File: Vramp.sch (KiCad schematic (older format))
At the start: 2 parts

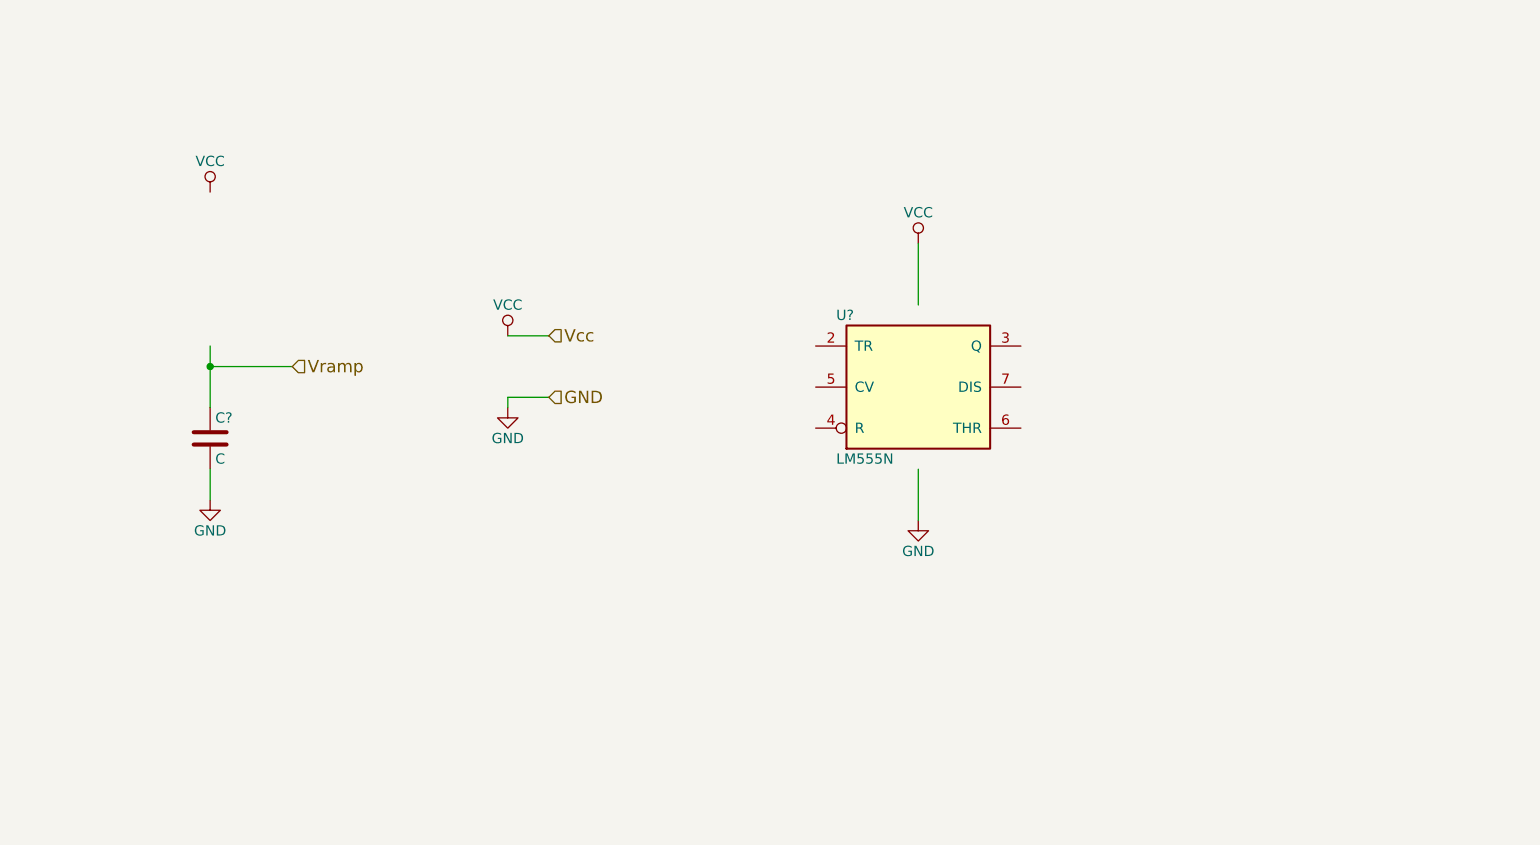
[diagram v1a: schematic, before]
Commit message: Created Ramp Voltage Source
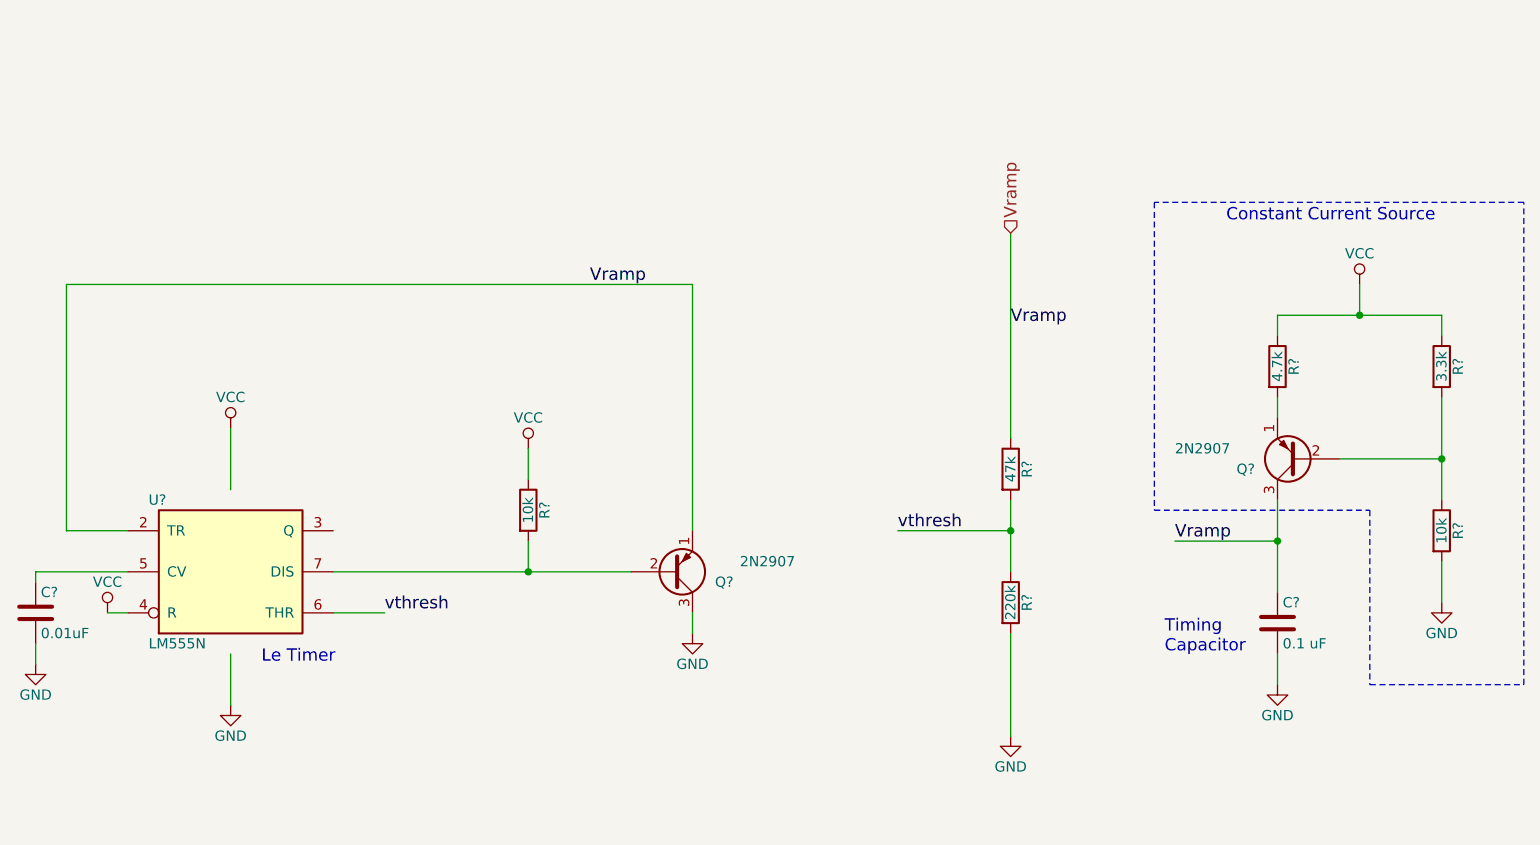
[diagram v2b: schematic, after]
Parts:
- added C?: 0.01uF, symbol C
- added Q? (x2): 2N2907, symbol Q_PNP_EBC
- added R? (x2): 10k, symbol R
- added R?: 4.7k, symbol R
- added R?: 3.3k, symbol R
- added R?: 47k, symbol R
- added R?: 220k, symbol R
- C?: value C -> 0.1 uF
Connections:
- net labels added: vthresh
- net labels removed: Vcc
- wire segments 8 -> 30
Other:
- note added: "Constant Current Source\n"
- note added: "Le Timer\n"
- note added: "Timing\nCapacitor\n"
- moved on the sheet: C?, U?

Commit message: Added some text to make things more obvious
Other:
- note added: "Charge Dumping\nCapacitor"
- moved on the sheet: C?, Q?, R?, U?

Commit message: Did a whole bunch of layout
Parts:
- C1, C2: renamed from C?; footprint (none) -> Capacitors_THT:C_Disc_D3_P2.5
- Q1, Q2: renamed from Q?; footprint (none) -> TO_SOT_Packages_THT:TO-18_3Pin
- R10, R11, R6, R7, R8, R9: renamed from R?; footprint (none) -> Resistors_THT:Resistor_Horizontal_RM7mm
- U4: renamed from U?; footprint (none) -> Housings_DIP:DIP-8_W7.62mm_LongPads
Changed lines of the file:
@@
 $Descr A4 11693 8268
 encoding utf-8
-Sheet 4 4
+Sheet 3 4
 Title ""
 Date ""
@@
 $EndDescr
 $Comp
-L GND #PWR?
+L GND #PWR012
 U 1 1 58B660FA
 P 8250 3850
-F 0 "#PWR?" H 8250 3600 50  0001 C CNN
+F 0 "#PWR012" H 8250 3600 50  0001 C CNN
 F 1 "GND" H 8250 3700 50  0000 C CNN
 F 2 "" H 8250 3850 50  0000 C CNN
@@
 $EndComp
 $Comp
-L C C?
+L C C2
 U 1 1 58B6610E
 P 8250 3550
-F 0 "C?" H 8275 3650 50  0000 L CNN
+F 0 "C2" H 8275 3650 50  0000 L CNN
 F 1 "0.1 uF" H 8275 3450 50  0000 L CNN
-F 2 "" H 8288 3400 50  0000 C CNN
+F 2 "Capacitors_THT:C_Disc_D3_P2.5" H 8288 3400 50  0001 C CNN
 F 3 "" H 8250 3550 50  0000 C CNN
 	1    8250 3550
@@
 	8250 2950 8250 3400
 $Comp
-L VCC #PWR?
+L VCC #PWR013
 U 1 1 58B662CB
 P 8650 1900
-F 0 "#PWR?" H 8650 1750 50  0001 C CNN
+F 0 "#PWR013" H 8650 1750 50  0001 C CNN
 F 1 "VCC" H 8650 2050 50  0000 C CNN
 F 2 "" H 8650 1900 50  0000 C CNN
@@
 $EndComp
 $Comp
-L LM555N U?
+L LM555N U4
 U 1 1 58B668DE
 P 3200 4600
-F 0 "U?" H 2800 4950 50  0000 L CNN
+F 0 "U4" H 2800 4950 50  0000 L CNN
 F 1 "LM555N" H 2800 4250 50  0000 L CNN
-F 2 "" H 3200 4600 50  0000 C CNN
+F 2 "Housings_DIP:DIP-8_W7.62mm_LongPads" H 3200 4600 50  0001 C CNN
 F 3 "" H 3200 4600 50  0000 C CNN
 	1    3200 4600
@@
 $EndComp
 $Comp
-L VCC #PWR?
+L VCC #PWR014
 U 1 1 58B669AB
 P 3200 3900
-F 0 "#PWR?" H 3200 3750 50  0001 C CNN
+F 0 "#PWR014" H 3200 3750 50  0001 C CNN
 F 1 "VCC" H 3200 4050 50  0000 C CNN
 F 2 "" H 3200 3900 50  0000 C CNN
@@
 $EndComp
 $Comp
-L GND #PWR?
+L GND #PWR015
 U 1 1 58B669D1
 P 3200 5250
-F 0 "#PWR?" H 3200 5000 50  0001 C CNN
+F 0 "#PWR015" H 3200 5000 50  0001 C CNN
 F 1 "GND" H 3200 5100 50  0000 C CNN
 F 2 "" H 3200 5250 50  0000 C CNN
@@
 	3200 5250 3200 5000
 $Comp
-L Q_PNP_EBC Q?
+L Q_PNP_EBC Q2
 U 1 1 58B73697
 P 8350 2750
-F 0 "Q?" H 8650 2800 50  0000 R CNN
+F 0 "Q2" H 8650 2800 50  0000 R CNN
 F 1 "2N2907" H 8950 2700 50  0000 R CNN
-F 2 "" H 8550 2850 50  0000 C CNN
+F 2 "TO_SOT_Packages_THT:TO-18_3Pin" H 8550 2850 50  0001 C CNN
 F 3 "" H 8350 2750 50  0000 C CNN
 	1    8350 2750
@@
 $EndComp
 $Comp
-L R R?
+L R R9
 U 1 1 58B736E3
 P 8250 2300
-F 0 "R?" V 8330 2300 50  0000 C CNN
+F 0 "R9" V 8330 2300 50  0000 C CNN
 F 1 "4.7k" V 8250 2300 50  0000 C CNN
-F 2 "" V 8180 2300 50  0000 C CNN
+F 2 "Resistors_THT:Resistor_Horizontal_RM7mm" V 8180 2300 50  0001 C CNN
 F 3 "" H 8250 2300 50  0000 C CNN
 	1    8250 2300
@@
 $EndComp
 $Comp
-L R R?
+L R R10
 U 1 1 58B73718
 P 9050 2300
-F 0 "R?" V 9130 2300 50  0000 C CNN
+F 0 "R10" V 9130 2300 50  0000 C CNN
 F 1 "3.3k" V 9050 2300 50  0000 C CNN
-F 2 "" V 8980 2300 50  0000 C CNN
+F 2 "Resistors_THT:Resistor_Horizontal_RM7mm" V 8980 2300 50  0001 C CNN
 F 3 "" H 9050 2300 50  0000 C CNN
 	1    9050 2300
@@
 	8250 2450 8250 2550
 $Comp
-L R R?
+L R R11
 U 1 1 58B736C8
 P 9050 3100
-F 0 "R?" V 9130 3100 50  0000 C CNN
+F 0 "R11" V 9130 3100 50  0000 C CNN
 F 1 "10k" V 9050 3100 50  0000 C CNN
-F 2 "" V 8980 3100 50  0000 C CNN
+F 2 "Resistors_THT:Resistor_Horizontal_RM7mm" V 8980 3100 50  0001 C CNN
 F 3 "" H 9050 3100 50  0000 C CNN
 	1    9050 3100
@@
 $EndComp
 $Comp
-L GND #PWR?
+L GND #PWR016
 U 1 1 58B736F6
 P 9050 3450
-F 0 "#PWR?" H 9050 3200 50  0001 C CNN
+F 0 "#PWR016" H 9050 3200 50  0001 C CNN
 F 1 "GND" H 9050 3300 50  0000 C CNN
 F 2 "" H 9050 3450 50  0000 C CNN
@@
 	2700 4400 2400 4400
 $Comp
-L VCC #PWR?
+L VCC #PWR017
 U 1 1 58B74027
 P 2600 4800
-F 0 "#PWR?" H 2600 4650 50  0001 C CNN
+F 0 "#PWR017" H 2600 4650 50  0001 C CNN
 F 1 "VCC" H 2600 4950 50  0000 C CNN
 F 2 "" H 2600 4800 50  0000 C CNN
@@
 	2700 4800 2600 4800
 $Comp
-L C C?
+L C C1
 U 1 1 58B74217
 P 2250 4800
-F 0 "C?" H 2275 4900 50  0000 L CNN
+F 0 "C1" H 2275 4900 50  0000 L CNN
 F 1 "0.01uF" H 2275 4700 50  0000 L CNN
-F 2 "" H 2288 4650 50  0000 C CNN
+F 2 "Capacitors_THT:C_Disc_D3_P2.5" H 2288 4650 50  0001 C CNN
 F 3 "" H 2250 4800 50  0000 C CNN
 	1    2250 4800
@@
 $EndComp
 $Comp
-L GND #PWR?
+L GND #PWR018
 U 1 1 58B7428F
 P 2250 5050
-F 0 "#PWR?" H 2250 4800 50  0001 C CNN
+F 0 "#PWR018" H 2250 4800 50  0001 C CNN
 F 1 "GND" H 2250 4900 50  0000 C CNN
 F 2 "" H 2250 5050 50  0000 C CNN
@@
 	2250 4600 2250 4650
 $Comp
-L Q_PNP_EBC Q?
+L Q_PNP_EBC Q1
 U 1 1 58B746E1
 P 5350 4600
-F 0 "Q?" H 5650 4650 50  0000 R CNN
+F 0 "Q1" H 5650 4650 50  0000 R CNN
 F 1 "2N2907" H 5950 4550 50  0000 R CNN
-F 2 "" H 5550 4700 50  0000 C CNN
+F 2 "TO_SOT_Packages_THT:TO-18_3Pin" H 5550 4700 50  0001 C CNN
 F 3 "" H 5350 4600 50  0000 C CNN
 	1    5350 4600
@@
 $EndComp
 $Comp
-L GND #PWR?
+L GND #PWR019
 U 1 1 58B7491D
 P 5450 4900
-F 0 "#PWR?" H 5450 4650 50  0001 C CNN
+F 0 "#PWR019" H 5450 4650 50  0001 C CNN
 F 1 "GND" H 5450 4750 50  0000 C CNN
 F 2 "" H 5450 4900 50  0000 C CNN
@@
 	3700 4600 5150 4600
 $Comp
-L VCC #PWR?
+L VCC #PWR020
 U 1 1 58B74D28
 P 4650 4000
-F 0 "#PWR?" H 4650 3850 50  0001 C CNN
+F 0 "#PWR020" H 4650 3850 50  0001 C CNN
 F 1 "VCC" H 4650 4150 50  0000 C CNN
 F 2 "" H 4650 4000 50  0000 C CNN
@@
 $EndComp
 $Comp
-L R R?
+L R R6
 U 1 1 58B74D4C
 P 4650 4300
-F 0 "R?" V 4730 4300 50  0000 C CNN
+F 0 "R6" V 4730 4300 50  0000 C CNN
 F 1 "10k" V 4650 4300 50  0000 C CNN
-F 2 "" V 4580 4300 50  0000 C CNN
+F 2 "Resistors_THT:Resistor_Horizontal_RM7mm" V 4580 4300 50  0001 C CNN
 F 3 "" H 4650 4300 50  0000 C CNN
 	1    4650 4300
@@
 Vramp
 $Comp
-L R R?
+L R R7
 U 1 1 58B7583F
 P 7000 3700
-F 0 "R?" V 7080 3700 50  0000 C CNN
+F 0 "R7" V 7080 3700 50  0000 C CNN
 F 1 "47k" V 7000 3700 50  0000 C CNN
-F 2 "" V 6930 3700 50  0000 C CNN
+F 2 "Resistors_THT:Resistor_Horizontal_RM7mm" V 6930 3700 50  0001 C CNN
 F 3 "" H 7000 3700 50  0000 C CNN
 	1    7000 3700
@@
 $EndComp
 $Comp
-L R R?
+L R R8
 U 1 1 58B75870
 P 7000 4350
-F 0 "R?" V 7080 4350 50  0000 C CNN
+F 0 "R8" V 7080 4350 50  0000 C CNN
 F 1 "220k" V 7000 4350 50  0000 C CNN
-F 2 "" V 6930 4350 50  0000 C CNN
+F 2 "Resistors_THT:Resistor_Horizontal_RM7mm" V 6930 4350 50  0001 C CNN
 F 3 "" H 7000 4350 50  0000 C CNN
 	1    7000 4350
@@
 	7000 4500 7000 5000
 $Comp
-L GND #PWR?
+L GND #PWR021
 U 1 1 58B75921
 P 7000 5000
-F 0 "#PWR?" H 7000 4750 50  0001 C CNN
+F 0 "#PWR021" H 7000 4750 50  0001 C CNN
 F 1 "GND" H 7000 4850 50  0000 C CNN
 F 2 "" H 7000 5000 50  0000 C CNN
